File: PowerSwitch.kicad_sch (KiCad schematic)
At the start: 16 parts, among them U401 BTT6010

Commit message: Update parts
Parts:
- C401, C402, C403, C404: footprint Capacitor_SMD:C_0603_1608Metric -> V2_Capacitor_SMD:C_0603; symbol Device:C_Small -> V2_Device:C_0603_0u1; Manufacturer (none) -> TDK; Mouser (none) -> 810-CGA3E2X7R1H104MA; Product (none) -> CGA3E2X7R1H104M080AA
- D401: footprint Diode_SMD:D_SOD-523 -> V2_Diode_SMD:D_SOD-523; Manufacaturer (none) -> ROHM Semiconductor; Manufacturer (none) -> ROHM Semiconductor; Mouser (none) -> 755-RB501SM-30FHT2R; Product (none) -> RB501SM-30FHT2R
- R401, R405, R406: footprint Resistor_SMD:R_0603_1608Metric -> V2_Resistor_SMD:R_0603; symbol Device:R_Small -> V2_Device:R_0603_100k; Manufacturer (none) -> Vishay; Mouser (none) -> 71-CRCW0603100KFKEAC; Product (none) -> CRCW0603100KFKEAC; Rating (none) -> 100mW
- R402, R403, R407, R408: footprint Resistor_SMD:R_0603_1608Metric -> V2_Resistor_SMD:R_0603; symbol Device:R_Small -> V2_Device:R_0603_10k; Manufacturer (none) -> Vishay; Mouser (none) -> 71-CRCW060310K0FKEAC; Product (none) -> CRCW060310K0FKEAC; Rating (none) -> 100mW
- R404: footprint Resistor_SMD:R_0603_1608Metric -> V2_Resistor_SMD:R_0603; symbol Device:R_Small -> V2_Device:R_0603_100R; Manufacturer (none) -> Vishay; Mouser (none) -> 71-CRCW0603100RFKEAH; Product (none) -> CRCW0603100RFKEAHP; Rating (none) -> 330mW
- R409, R410: footprint Resistor_SMD:R_0603_1608Metric -> V2_Resistor_SMD:R_0603; symbol Device:R_Small -> V2_Device:R_0603_2k7; Manufacturer (none) -> Vishay; Mouser (none) -> 71-CRCW06032K70FKEAC; Product (none) -> CRCW06032K70FKEAC; Rating (none) -> 100mW
- U401: Manufacturer (none) -> Infineon; Mouser (none) -> 726-BTT60101ERBXUMA1; Product (none) -> BTT60101ERBXUMA1

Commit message: Update library
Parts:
- C401, C402, C403, C404: Rating (none) -> 50V
- D401: Manufacaturer ROHM Semiconductor -> (none)
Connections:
- net +24V renamed +28V
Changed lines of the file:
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@@
 	)
 	(symbol
-		(lib_id "V2_power:+24V")
+		(lib_id "V2_power:+28V")
 		(at 166.37 44.45 0)
 		(unit 1)
@@
 			)
 		)
-		(property "Value" "+24V"
+		(property "Value" "+28V"
 			(at 166.37 39.37 0)
 			(effects
@@
 			)
 		)
-		(property "Description" "Power symbol creates a global label with name \"+24V\""
+		(property "Description" ""
 			(at 166.37 44.45 0)
 			(effects
@@
 			)
 		)
-		(property "Description" "Power symbol creates a global label with name \"GND\" , ground"
+		(property "Description" ""
 			(at 191.77 57.15 0)
 			(effects
@@
 			)
 		)
-		(property "Sim.Pin" ""
-			(at 121.92 121.92 90)
-			(effects
-				(font
-					(size 1.27 1.27)
-				)
-				(hide yes)
-			)
-		)
 		(property "Product" "CRCW060310K0FKEAC"
 			(at 104.14 121.92 0)
@@
 			)
 		)
-		(property "Sim.Pin" ""
-			(at 114.3 132.08 90)
-			(effects
-				(font
-					(size 1.27 1.27)
-				)
-				(hide yes)
-			)
-		)
 		(property "Product" "CRCW060310K0FKEAC"
 			(at 132.08 132.08 0)
@@
 			)
 		)
-		(property "Description" "Power symbol creates a global label with name \"GND\" , ground"
+		(property "Description" ""
 			(at 127 137.16 0)
 			(effects
@@
 			)
 		)
-		(property "Sim.Pin" ""
-			(at 181.61 52.07 90)
-			(effects
-				(font
-					(size 1.27 1.27)
-				)
-				(hide yes)
-			)
-		)
 		(property "Product" "CRCW060310K0FKEAC"
 			(at 199.39 52.07 0)
@@
 			)
 		)
-		(property "Description" "Power symbol creates a global label with name \"GND\" , ground"
+		(property "Description" ""
 			(at 184.15 121.92 0)
 			(effects
@@
 			)
 		)
-		(property "Description" "Power symbol creates a global label with name \"GND\" , ground"
+		(property "Description" ""
 			(at 107.95 116.84 0)
 			(effects
@@
 			)
 		)
-		(property "Sim.Pin" ""
-			(at 127 134.62 0)
-			(effects
-				(font
-					(size 1.27 1.27)
-				)
-				(hide yes)
-			)
-		)
 		(property "Product" "CRCW06032K70FKEAC"
 			(at 127 154.94 0)
@@
 			)
 		)
-		(property "Description" "Power symbol creates a global label with name \"GND\" , ground"
+		(property "Description" ""
 			(at 184.15 105.41 0)
 			(effects
@@
 			)
 		)
-		(property "Description" "Power symbol creates a global label with name \"+3V3\""
+		(property "Description" ""
 			(at 166.37 92.71 0)
 			(effects
@@
 			)
 		)
-		(property "Sim.Pin" ""
-			(at 166.37 54.61 0)
-			(effects
-				(font
-					(size 1.27 1.27)
-				)
-				(hide yes)
-			)
-		)
 		(property "Product" "CRCW060310K0FKEAC"
 			(at 166.37 72.39 0)
@@
 			)
 		)
-		(property "Sim.Pin" ""
-			(at 166.37 46.99 0)
-			(effects
-				(font
-					(size 1.27 1.27)
-				)
-				(hide yes)
-			)
-		)
 		(property "Rating" "100mW"
 			(at 166.37 67.31 0)
@@
 			)
 		)
-		(property "Description" "Power symbol creates a global label with name \"GND\" , ground"
+		(property "Description" ""
 			(at 156.21 132.08 0)
 			(effects
@@
 			)
 		)
-		(property "Sim.Pin" ""
-			(at 184.15 119.38 0)
-			(effects
-				(font
-					(size 1.27 1.27)
-				)
-				(hide yes)
-			)
-		)
 		(property "Manufacturer" "TDK"
 			(at 184.15 134.62 0)
@@
 			)
 		)
+		(property "Rating" "50V"
+			(at 184.15 142.24 0)
+			(effects
+				(font
+					(size 1.27 1.27)
+				)
+				(hide yes)
+			)
+		)
 		(pin "1"
 		)
@@
 			)
 		)
-		(property "Sim.Pin" ""
-			(at 146.05 124.46 0)
-			(effects
-				(font
-					(size 1.27 1.27)
-				)
-				(hide yes)
-			)
-		)
 		(property "Manufacturer" "Infineon"
 			(at 146.05 167.64 0)
@@
 	)
 	(symbol
-		(lib_id "V2_power:+24V")
+		(lib_id "V2_power:+28V")
 		(at 135.89 116.84 90)
 		(unit 1)
@@
 			)
 		)
-		(property "Value" "+24V"
+		(property "Value" "+28V"
 			(at 132.08 116.8399 90)
 			(effects
@@
 			)
 		)
-		(property "Description" "Power symbol creates a global label with name \"+24V\""
+		(property "Description" ""
 			(at 135.89 116.84 0)
 			(effects
@@
 			)
 		)
-		(property "Sim.Pin" ""
-			(at 105.41 116.84 90)
-			(effects
-				(font
-					(size 1.27 1.27)
-				)
-				(hide yes)
-			)
-		)
 		(property "Rating" "100mW"
 			(at 85.09 116.84 0)
@@
 			)
 		)
-		(property "Sim.Pin" ""
-			(at 158.75 119.38 0)
-			(effects
-				(font
-					(size 1.27 1.27)
-				)
-				(hide yes)
-			)
-		)
 		(property "Rating" "100mW"
 			(at 158.75 139.7 0)
@@
 			)
 		)
-		(property "Sim.Pin" ""
-			(at 166.37 95.25 0)
-			(effects
-				(font
-					(size 1.27 1.27)
-				)
-				(hide yes)
-			)
-		)
 		(property "Rating" "330mW"
 			(at 166.37 118.11 0)
@@
 			)
 		)
-		(property "Description" "Power symbol creates a global label with name \"GND\" , ground"
+		(property "Description" ""
 			(at 135.89 137.16 0)
 			(effects
@@
 			)
 		)
-		(property "Description" "Power symbol creates a global label with name \"GND\" , ground"
+		(property "Description" ""
 			(at 166.37 57.15 0)
 			(effects
@@
 			)
 		)
-		(property "Sim.Pin" ""
-			(at 166.37 102.87 90)
-			(effects
-				(font
-					(size 1.27 1.27)
-				)
-				(hide yes)
-			)
-		)
 		(property "Product" "RB501SM-30FHT2R"
 			(at 179.07 102.87 0)
@@
 			)
 		)
-		(property "Manufacaturer" "ROHM Semiconductor"
-			(at 176.53 102.87 0)
-			(effects
-				(font
-					(size 1.27 1.27)
-				)
-				(hide yes)
-			)
-		)
 		(property "Manufacturer" "ROHM Semiconductor"
 			(at 176.53 102.87 0)
@@
 			)
 		)
-		(property "Sim.Pin" ""
-			(at 135.89 134.62 0)
-			(effects
-				(font
-					(size 1.27 1.27)
-				)
-				(hide yes)
-			)
-		)
 		(property "Product" "CRCW06032K70FKEAC"
 			(at 135.89 154.94 0)
@@
 			)
 		)
-		(property "Description" "Power symbol creates a global label with name \"GND\" , ground"
+		(property "Description" ""
 			(at 158.75 121.92 0)
 			(effects
@@
 			)
 		)
-		(property "Sim.Pin" ""
-			(at 107.95 134.62 0)
-			(effects
-				(font
-					(size 1.27 1.27)
-				)
-				(hide yes)
-			)
-		)
 		(property "Manufacturer" "TDK"
 			(at 107.95 149.86 0)
@@
 			)
 		)
+		(property "Rating" "50V"
+			(at 107.95 157.48 0)
+			(effects
+				(font
+					(size 1.27 1.27)
+				)
+				(hide yes)
+			)
+		)
 		(pin "1"
 		)
@@
 			)
 		)
-		(property "Description" "Power symbol creates a global label with name \"GND\" , ground"
+		(property "Description" ""
 			(at 107.95 137.16 0)
 			(effects
@@
 			)
 		)
-		(property "Sim.Pin" ""
-			(at 184.15 102.87 0)
-			(effects
-				(font
-					(size 1.27 1.27)
-				)
-				(hide yes)
-			)
-		)
 		(property "Manufacturer" "TDK"
 			(at 184.15 118.11 0)
@@
 			)
 		)
+		(property "Rating" "50V"
+			(at 184.15 125.73 0)
+			(effects
+				(font
+					(size 1.27 1.27)
+				)
+				(hide yes)
+			)
+		)
 		(pin "1"
 		)
@@
 			)
 		)
-		(property "Sim.Pin" ""
-			(at 191.77 54.61 0)
-			(effects
-				(font
-					(size 1.27 1.27)
-				)
-				(hide yes)
-			)
-		)
 		(property "Manufacturer" "TDK"
 			(at 191.77 69.85 0)
@@
 			)
 		)
+		(property "Rating" "50V"
+			(at 191.77 77.47 0)
+			(effects
+				(font
+					(size 1.27 1.27)
+				)
+				(hide yes)
+			)
+		)
 		(pin "1"
 		)
@@
 			)
 		)
-		(property "Description" "Power symbol creates a global label with name \"+3V3\""
+		(property "Description" ""
 			(at 135.89 127 0)
 			(effects

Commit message: Update Library
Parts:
- C401, C402, C403, C404: symbol V2_Device:C_0603_0u1 -> V2_Capacitor:0603_0u1
- R401, R405, R406: symbol V2_Device:R_0603_100k -> V2_Resistor:0603_100k
- R402, R403, R407, R408: symbol V2_Device:R_0603_10k -> V2_Resistor:0603_10k
- R404: symbol V2_Device:R_0603_100R -> V2_Resistor:0603_100R
- R409, R410: symbol V2_Device:R_0603_2k7 -> V2_Resistor:0603_2k7
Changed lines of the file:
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@@
 	)
 	(symbol
-		(lib_id "V2_Device:R_0603_10k")
+		(lib_id "V2_Resistor:0603_10k")
 		(at 121.92 121.92 270)
 		(unit 1)
@@
 	)
 	(symbol
-		(lib_id "V2_Device:R_0603_10k")
+		(lib_id "V2_Resistor:0603_10k")
 		(at 114.3 132.08 90)
 		(unit 1)
@@
 	)
 	(symbol
-		(lib_id "V2_Device:R_0603_10k")
+		(lib_id "V2_Resistor:0603_10k")
 		(at 181.61 52.07 90)
 		(unit 1)
@@
 	)
 	(symbol
-		(lib_id "V2_Device:R_0603_2k7")
+		(lib_id "V2_Resistor:0603_2k7")
 		(at 127 134.62 0)
 		(unit 1)
@@
 	)
 	(symbol
-		(lib_id "V2_Device:R_0603_10k")
+		(lib_id "V2_Resistor:0603_10k")
 		(at 166.37 54.61 0)
 		(unit 1)
@@
 	)
 	(symbol
-		(lib_id "V2_Device:R_0603_100k")
+		(lib_id "V2_Resistor:0603_100k")
 		(at 166.37 46.99 0)
 		(unit 1)
@@
 	)
 	(symbol
-		(lib_id "V2_Device:C_0603_0u1")
+		(lib_id "V2_Capacitor:0603_0u1")
 		(at 184.15 119.38 0)
 		(unit 1)
@@
 	)
 	(symbol
-		(lib_id "V2_Device:R_0603_100k")
+		(lib_id "V2_Resistor:0603_100k")
 		(at 105.41 116.84 270)
 		(unit 1)
@@
 	)
 	(symbol
-		(lib_id "V2_Device:R_0603_100k")
+		(lib_id "V2_Resistor:0603_100k")
 		(at 158.75 119.38 0)
 		(unit 1)
@@
 	)
 	(symbol
-		(lib_id "V2_Device:R_0603_100R")
+		(lib_id "V2_Resistor:0603_100R")
 		(at 166.37 95.25 0)
 		(unit 1)
@@
 	)
 	(symbol
-		(lib_id "V2_Device:R_0603_2k7")
+		(lib_id "V2_Resistor:0603_2k7")
 		(at 135.89 134.62 0)
 		(unit 1)
@@
 	)
 	(symbol
-		(lib_id "V2_Device:C_0603_0u1")
+		(lib_id "V2_Capacitor:0603_0u1")
 		(at 107.95 134.62 0)
 		(unit 1)
@@
 	)
 	(symbol
-		(lib_id "V2_Device:C_0603_0u1")
+		(lib_id "V2_Capacitor:0603_0u1")
 		(at 184.15 102.87 0)
 		(unit 1)
@@
 	)
 	(symbol
-		(lib_id "V2_Device:C_0603_0u1")
+		(lib_id "V2_Capacitor:0603_0u1")
 		(at 191.77 54.61 0)
 		(unit 1)

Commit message: Replace diode
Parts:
- U401: Rating (none) -> 36V
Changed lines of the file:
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@@
 		(on_board yes)
 		(dnp no)
-		(property "Reference" "#PWR0401"
+		(property "Reference" "#PWR401"
 			(at 166.37 48.26 0)
 			(effects
@@
 			(project "hihat-1"
 				(path "/6c8448b4-b04d-47e1-934e-e40cbe27a7be/ba748654-beb9-4861-aa35-c19e08caaf2e"
-					(reference "#PWR0401")
+					(reference "#PWR401")
 					(unit 1)
 				)
@@
 		(on_board yes)
 		(dnp no)
-		(property "Reference" "#PWR0403"
+		(property "Reference" "#PWR403"
 			(at 191.77 63.5 0)
 			(effects
@@
 			(project "pulse"
 				(path "/6c8448b4-b04d-47e1-934e-e40cbe27a7be/ba748654-beb9-4861-aa35-c19e08caaf2e"
-					(reference "#PWR0403")
+					(reference "#PWR403")
 					(unit 1)
 				)
@@
 			)
 		)
-		(property "Description" "Resistor, small symbol"
+		(property "Description" ""
 			(at 109.728 121.92 0)
 			(effects
@@
 			)
 		)
-		(property "Description" "Resistor, small symbol"
+		(property "Description" ""
 			(at 126.492 132.08 0)
 			(effects
@@
 		(on_board yes)
 		(dnp no)
-		(property "Reference" "#PWR0413"
+		(property "Reference" "#PWR413"
 			(at 127 143.51 0)
 			(effects
@@
 			(project "pulse"
 				(path "/6c8448b4-b04d-47e1-934e-e40cbe27a7be/ba748654-beb9-4861-aa35-c19e08caaf2e"
-					(reference "#PWR0413")
+					(reference "#PWR413")
 					(unit 1)
 				)
@@
 			)
 		)
-		(property "Description" "Resistor, small symbol"
+		(property "Description" ""
 			(at 193.802 52.07 0)
 			(effects
@@
 		(on_board yes)
 		(dnp no)
-		(property "Reference" "#PWR0409"
+		(property "Reference" "#PWR409"
 			(at 184.15 128.27 0)
 			(effects
@@
 			(project "pulse"
 				(path "/6c8448b4-b04d-47e1-934e-e40cbe27a7be/ba748654-beb9-4861-aa35-c19e08caaf2e"
-					(reference "#PWR0409")
+					(reference "#PWR409")
 					(unit 1)
 				)
@@
 		(on_board yes)
 		(dnp no)
-		(property "Reference" "#PWR0406"
+		(property "Reference" "#PWR406"
 			(at 114.3 116.84 0)
 			(effects
@@
 			(project "pulse"
 				(path "/6c8448b4-b04d-47e1-934e-e40cbe27a7be/ba748654-beb9-4861-aa35-c19e08caaf2e"
-					(reference "#PWR0406")
+					(reference "#PWR406")
 					(unit 1)
 				)
@@
 			)
 		)
-		(property "Description" "Resistor, small symbol"
+		(property "Description" ""
 			(at 127 146.812 0)
 			(effects
@@
 		(on_board yes)
 		(dnp no)
-		(property "Reference" "#PWR0405"
+		(property "Reference" "#PWR405"
 			(at 184.15 111.76 0)
 			(effects
@@
 			(project "pulse"
 				(path "/6c8448b4-b04d-47e1-934e-e40cbe27a7be/ba748654-beb9-4861-aa35-c19e08caaf2e"
-					(reference "#PWR0405")
+					(reference "#PWR405")
 					(unit 1)
 				)
@@
 		(on_board yes)
 		(dnp no)
-		(property "Reference" "#PWR0404"
+		(property "Reference" "#PWR404"
 			(at 166.37 96.52 0)
 			(effects
@@
 			(project "pulse"
 				(path "/6c8448b4-b04d-47e1-934e-e40cbe27a7be/ba748654-beb9-4861-aa35-c19e08caaf2e"
-					(reference "#PWR0404")
+					(reference "#PWR404")
 					(unit 1)
 				)
@@
 			)
 		)
-		(property "Description" "Resistor, small symbol"
+		(property "Description" ""
 			(at 166.37 66.802 0)
 			(effects
@@
 			)
 		)
-		(property "Description" "Resistor, small symbol"
+		(property "Description" ""
 			(at 166.37 59.182 0)
 			(effects
@@
 		(on_board yes)
 		(dnp no)
-		(property "Reference" "#PWR0411"
+		(property "Reference" "#PWR411"
 			(at 162.56 132.08 0)
 			(effects
@@
 			(project "pulse"
 				(path "/6c8448b4-b04d-47e1-934e-e40cbe27a7be/ba748654-beb9-4861-aa35-c19e08caaf2e"
-					(reference "#PWR0411")
+					(reference "#PWR411")
 					(unit 1)
 				)
@@
 			)
 		)
-		(property "Description" "Unpolarized capacitor, small symbol"
+		(property "Description" ""
 			(at 184.15 132.842 0)
 			(effects
@@
 			)
 		)
-		(property "Description" "Infineon Smart High Sde Switches PROFET™+ 24V"
+		(property "Description" "Infineon Smart High Side Switches PROFET™+ 24V"
 			(at 146.05 124.46 0)
 			(effects
@@
 			)
 		)
+		(property "Rating" "36V"
+			(at 146.05 175.26 0)
+			(effects
+				(font
+					(size 1.27 1.27)
+				)
+				(hide yes)
+			)
+		)
 		(pin "1"
 		)
@@
 		(dnp no)
 		(fields_autoplaced yes)
-		(property "Reference" "#PWR0407"
+		(property "Reference" "#PWR407"
 			(at 139.7 116.84 0)
 			(effects
@@
 			(project ""
 				(path "/6c8448b4-b04d-47e1-934e-e40cbe27a7be/ba748654-beb9-4861-aa35-c19e08caaf2e"
-					(reference "#PWR0407")
+					(reference "#PWR407")
 					(unit 1)
 				)
@@
 			)
 		)
-		(property "Description" "Resistor, small symbol"
+		(property "Description" ""
 			(at 93.218 116.84 0)
 			(effects
@@
 			)
 		)
-		(property "Description" "Resistor, small symbol"
+		(property "Description" ""
 			(at 158.75 131.572 0)
 			(effects
@@
 			)
 		)
-		(property "Description" "Resistor, small symbol"
+		(property "Description" ""
 			(at 166.37 107.442 0)
 			(effects
@@
 		(on_board yes)
 		(dnp no)
-		(property "Reference" "#PWR0414"
+		(property "Reference" "#PWR414"
 			(at 135.89 143.51 0)
 			(effects
@@
 			(project "pulse"
 				(path "/6c8448b4-b04d-47e1-934e-e40cbe27a7be/ba748654-beb9-4861-aa35-c19e08caaf2e"
-					(reference "#PWR0414")
+					(reference "#PWR414")
 					(unit 1)
 				)
@@
 		(on_board yes)
 		(dnp no)
-		(property "Reference" "#PWR0402"
+		(property "Reference" "#PWR402"
 			(at 166.37 63.5 0)
 			(effects
@@
 			(project "pulse"
 				(path "/6c8448b4-b04d-47e1-934e-e40cbe27a7be/ba748654-beb9-4861-aa35-c19e08caaf2e"
-					(reference "#PWR0402")
+					(reference "#PWR402")
 					(unit 1)
 				)
@@
 			)
 		)
-		(property "Description" "Resistor, small symbol"
+		(property "Description" ""
 			(at 135.89 146.812 0)
 			(effects
@@
 		(on_board yes)
 		(dnp no)
-		(property "Reference" "#PWR0408"
+		(property "Reference" "#PWR408"
 			(at 158.75 128.27 0)
 			(effects
@@
 			(project "pulse"
 				(path "/6c8448b4-b04d-47e1-934e-e40cbe27a7be/ba748654-beb9-4861-aa35-c19e08caaf2e"
-					(reference "#PWR0408")
+					(reference "#PWR408")
 					(unit 1)
 				)
@@
 			)
 		)
-		(property "Description" "Unpolarized capacitor, small symbol"
+		(property "Description" ""
 			(at 107.95 148.082 0)
 			(effects
@@
 		(on_board yes)
 		(dnp no)
-		(property "Reference" "#PWR0412"
+		(property "Reference" "#PWR412"
 			(at 107.95 143.51 0)
 			(effects
@@
 			(project "pulse"
 				(path "/6c8448b4-b04d-47e1-934e-e40cbe27a7be/ba748654-beb9-4861-aa35-c19e08caaf2e"
-					(reference "#PWR0412")
+					(reference "#PWR412")
 					(unit 1)
 				)
@@
 			)
 		)
-		(property "Description" "Unpolarized capacitor, small symbol"
+		(property "Description" ""
 			(at 184.15 116.332 0)
 			(effects
@@
 			)
 		)
-		(property "Description" "Unpolarized capacitor, small symbol"
+		(property "Description" ""
 			(at 191.77 68.072 0)
 			(effects
@@
 		(on_board yes)
 		(dnp no)
-		(property "Reference" "#PWR0410"
+		(property "Reference" "#PWR410"
 			(at 139.7 127 0)
 			(effects
@@
 			(project "pulse"
 				(path "/6c8448b4-b04d-47e1-934e-e40cbe27a7be/ba748654-beb9-4861-aa35-c19e08caaf2e"
-					(reference "#PWR0410")
-					(unit 1)
-				)
+					(reference "#PWR410")
+					(unit 1)
+				)

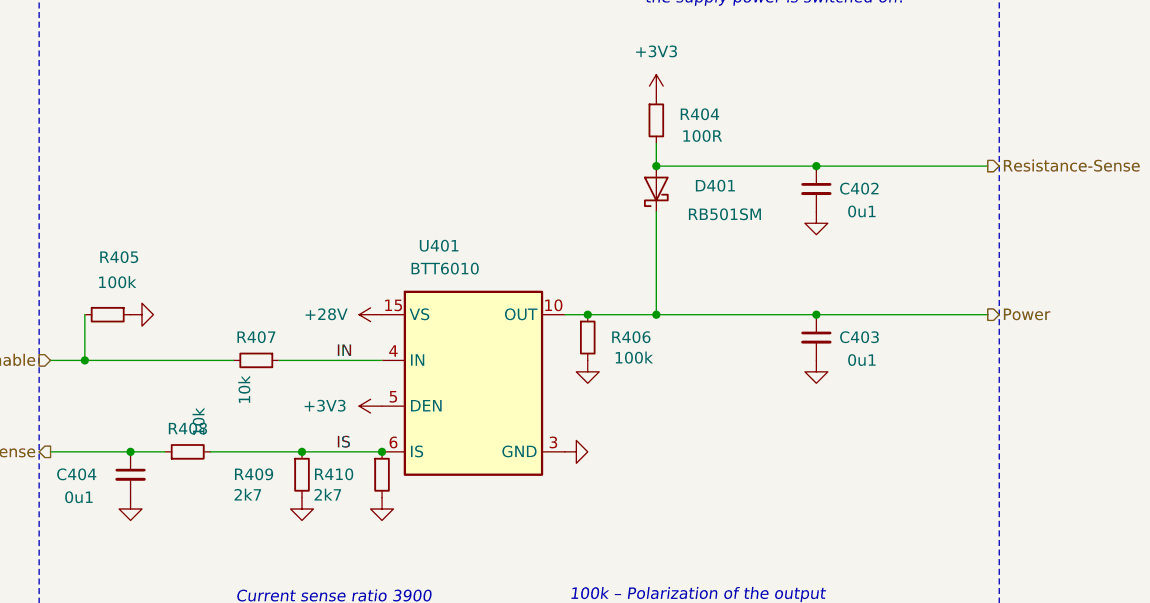
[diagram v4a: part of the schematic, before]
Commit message: Replace diode
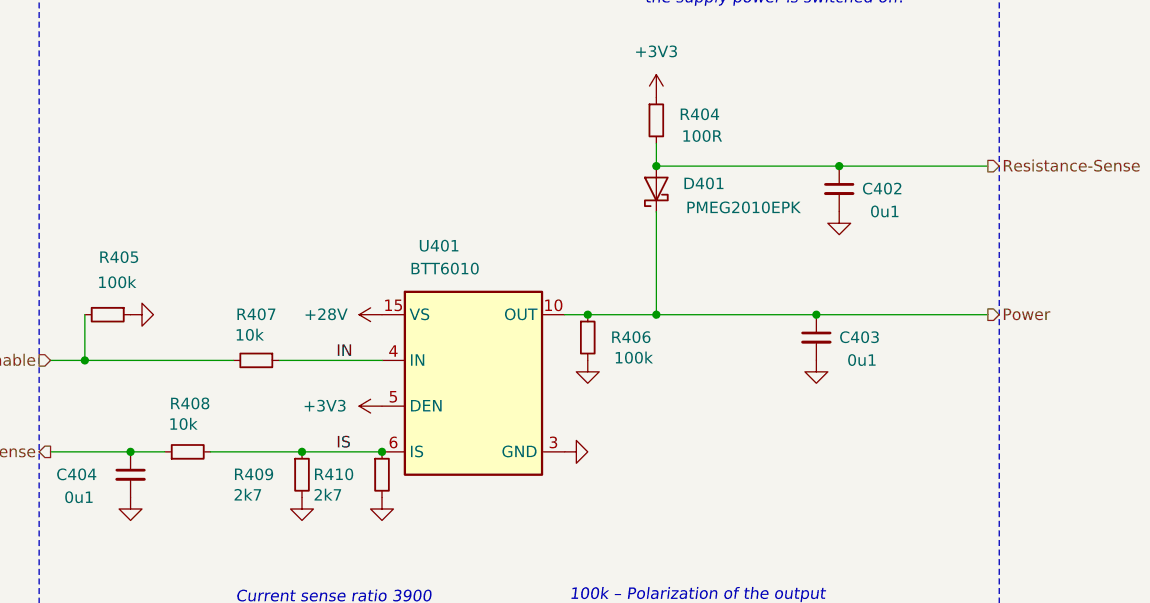
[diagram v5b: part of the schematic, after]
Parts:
- D401: value RB501SM -> PMEG2010EPK; footprint V2_Diode_SMD:D_SOD-523 -> V2_Diode_SMD:D_SOD-1608; symbol V2_Diode:RB501SM -> V2_Diode:PMEG2010EPK; Manufacturer ROHM Semiconductor -> Nexperia; Mouser 755-RB501SM-30FHT2R -> 771-PMEG2010EPK; Product RB501SM-30FHT2R -> PMEG2010EPK; Rating (none) -> 20V
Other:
- title: Power Switch -> V2 drum
- moved on the sheet: C402

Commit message: Update
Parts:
- C401: renamed from C404; Id (none) -> Capacitor:${SYMBOL_NAME}
- C402: renamed from C403; Id (none) -> Capacitor:${SYMBOL_NAME}
- C403: renamed from C402; Id (none) -> Capacitor:${SYMBOL_NAME}
- C404: renamed from C401; Id (none) -> Capacitor:${SYMBOL_NAME}
- D401: Id (none) -> Diode:${SYMBOL_NAME}
- R401: renamed from R405; Id (none) -> Resistor:${SYMBOL_NAME}
- R402: renamed from R408; Id (none) -> Resistor:${SYMBOL_NAME}
- R403: renamed from R407; Id (none) -> Resistor:${SYMBOL_NAME}
- R404: renamed from R409; Id (none) -> Resistor:${SYMBOL_NAME}
- R405: renamed from R410; Id (none) -> Resistor:${SYMBOL_NAME}
- R406: Id (none) -> Resistor:${SYMBOL_NAME}
- R407: renamed from R401; Id (none) -> Resistor:${SYMBOL_NAME}
- R408: renamed from R403; Id (none) -> Resistor:${SYMBOL_NAME}
- R409: renamed from R404; Id (none) -> Resistor:${SYMBOL_NAME}
- R410: renamed from R402; Id (none) -> Resistor:${SYMBOL_NAME}
- U401: Id (none) -> PowerSwitch:${SYMBOL_NAME}
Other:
- company: (none) -> Versio Duo
